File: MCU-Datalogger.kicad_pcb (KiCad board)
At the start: 2 copper layers, 0 parts

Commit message: Populate NewPCB
Imported the schematic into newPCB. This made also add the 3D model for all of the components.
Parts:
- added BT1: Battery, Connector_PinHeader_2.54mm:PinHeader_1x02_P2.54mm_Vertical, F.Cu at (121.8, 98.4)
- added C1: 0.1uF, Capacitor_SMD:C_0805_2012Metric, F.Cu at (143.8, 88.5)
- added C2: 22pF, Capacitor_SMD:C_0805_2012Metric, F.Cu at (143.8, 91.5)
- added C3: 22pF, Capacitor_SMD:C_0805_2012Metric, F.Cu at (143.8, 94.5)
- added C4: 0.1uF, Capacitor_SMD:C_0805_2012Metric, F.Cu at (143.8, 97.6)
- added C5: 100nF, Capacitor_SMD:C_0805_2012Metric, F.Cu at (143.8, 100.6)
- added D1: LED, LED_SMD:LED_0805_2012Metric, F.Cu at (148.3, 88.5)
- added D2: LED, LED_SMD:LED_0805_2012Metric, F.Cu at (148.3, 91.6)
- added H1: MountingHole, MountingHole:MountingHole_2.1mm, F.Cu at (122.4, 76.0)
- added H2: MountingHole, MountingHole:MountingHole_2.1mm, F.Cu at (122.4, 81.7)
- added H3: MountingHole, MountingHole:MountingHole_2.1mm, F.Cu at (122.4, 87.5)
- added H4: MountingHole, MountingHole:MountingHole_2.1mm, F.Cu at (122.4, 93.2)
- added J1: Conn_01x04_Pin, Connector_PinHeader_2.54mm:PinHeader_1x04_P2.54mm_Vertical, F.Cu at (162.7, 75.4)
- added J2: Conn_01x04_Pin, Connector_PinHeader_2.54mm:PinHeader_1x04_P2.54mm_Vertical, F.Cu at (167.2, 75.4)
- added J3: Conn_01x09_Pin, Connector_PinHeader_2.54mm:PinHeader_1x09_P2.54mm_Vertical_SMD_Pin1Left, F.Cu at (156.4, 85.6)
- added J4: Conn_02x03_Odd_Even, Connector_PinHeader_2.54mm:PinHeader_2x03_P2.54mm_Vertical, F.Cu at (162.7, 87.6)
- added R1: 10K, Resistor_SMD:R_0805_2012Metric, F.Cu at (127.5, 74.6)
- added R2: 10K, Resistor_SMD:R_0805_2012Metric, F.Cu at (127.5, 77.5)
- added R3: 4.7K, Resistor_SMD:R_0805_2012Metric, F.Cu at (127.5, 80.5)
- added R4: 4.7K, Resistor_SMD:R_0805_2012Metric, F.Cu at (127.5, 83.4)
- added R5: 330, Resistor_SMD:R_0805_2012Metric, F.Cu at (127.5, 86.4)
- added R6: 10K, Resistor_SMD:R_0805_2012Metric, F.Cu at (127.5, 89.3)
- added R7: 330, Resistor_SMD:R_0805_2012Metric, F.Cu at (127.5, 92.3)
- added U1: 24LC1025, Package_SO:SOIC-8_5.3x5.3mm_P1.27mm, F.Cu at (134.9, 76.6)
- added U2: 24LC1025, Package_SO:SOIC-8_5.3x5.3mm_P1.27mm, F.Cu at (134.9, 83.6)
- added U3: DS1337S_, DS1337S:SOIC127P600X175-8N, F.Cu at (134.8, 101.8)
- added U4: ATMEGA328PB-AU, ATMEGA328P-AU:QFP80P900X900X120-32N, F.Cu at (135.8, 92.8)
- added Y1: Crystal, Crystal:Crystal_SMD_5032-2Pin_5.0x3.2mm_HandSoldering, F.Cu at (145.2, 75.7)
- added Y2: 16 MHz, Crystal:Crystal_SMD_5032-2Pin_5.0x3.2mm_HandSoldering, F.Cu at (145.2, 81.0)

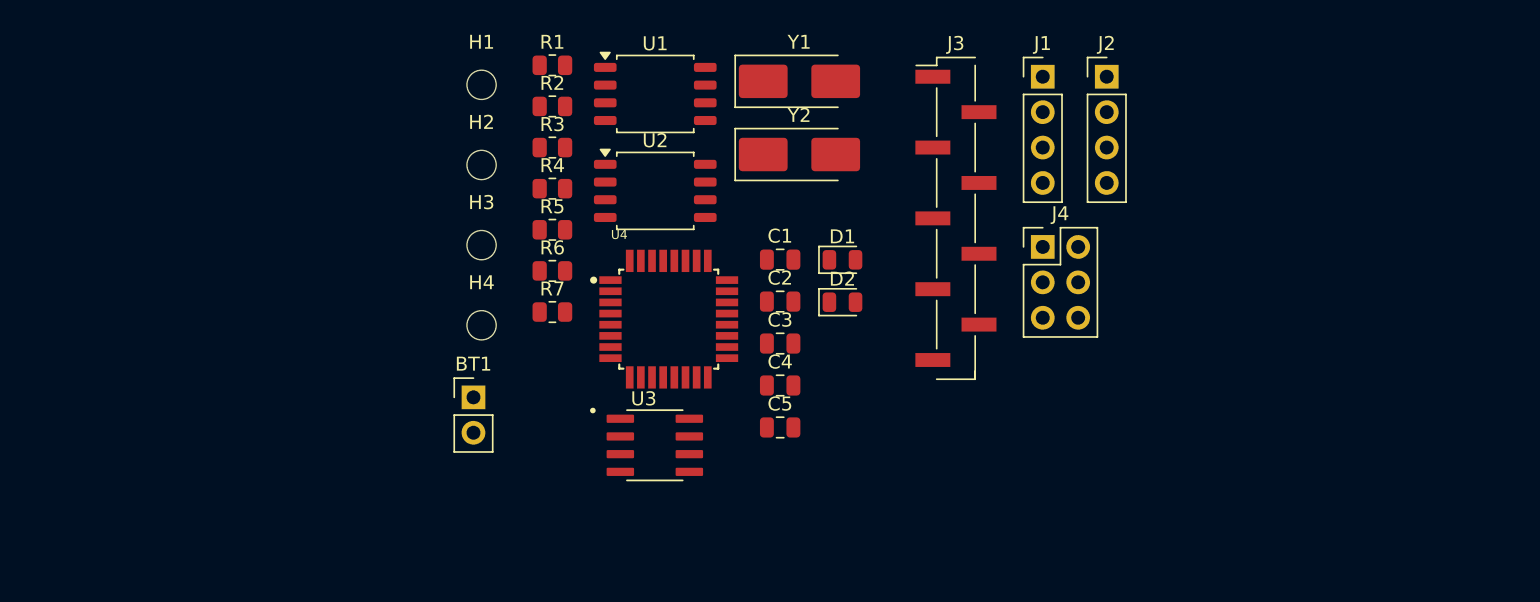
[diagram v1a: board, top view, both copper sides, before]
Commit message: Constraint
Add edge cut to NewPCB drawing
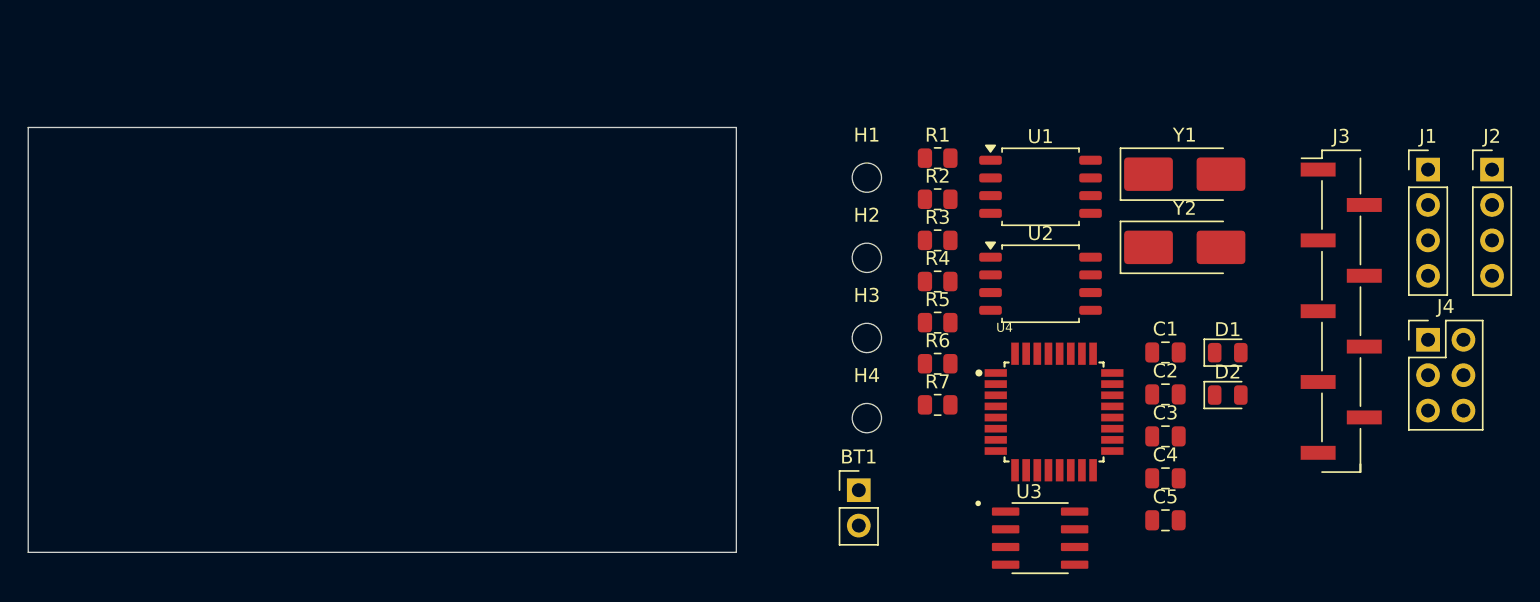
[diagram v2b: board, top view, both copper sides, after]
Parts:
- moved H1 28.4 mm to (150.0, 82.7)
- moved H2 28.4 mm to (150.0, 88.4)
- moved H3 28.4 mm to (150.0, 94.2)
- moved H4 28.4 mm to (150.0, 99.9)
- moved J1 28.4 mm to (190.3, 82.1)
- moved J2 28.4 mm to (194.9, 82.1)
- moved J3 28.4 mm to (184.1, 92.2)
- moved J4 28.4 mm to (190.3, 94.3)
- moved U4 28.4 mm to (163.5, 99.5)
- moved BT1 28.4 mm to (149.5, 105.1)
- moved R1 28.4 mm to (155.1, 81.2)
- moved R2 28.4 mm to (155.1, 84.2)
- moved R3 28.4 mm to (155.1, 87.2)
- moved R4 28.4 mm to (155.1, 90.1)
- moved R5 28.4 mm to (155.1, 93.0)
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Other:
- board outline added: 50.8 x 30.5 mm
